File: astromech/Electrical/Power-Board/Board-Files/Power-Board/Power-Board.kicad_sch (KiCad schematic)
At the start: 74 parts, among them J1 BAT_IN_SCREW, J10 HEAD_MOT, J2 BAT_IN_HOLE, J5 E_STOP, J6 CTRL_BRD, J7 JETSON, J8 L_DRIVE, J9 R_DRIVE, Q1 Q_NMOS_DSG, Q2 Q_NMOS_DSG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

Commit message: assigned some footprints
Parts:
- 12V1, 12V2, 12V3, 12V4, 3.3V1, 3.3V2, 3.3V3, 3.3V4, 5V1, 5V2, 5V3, 5V4: footprint (none) -> astromech-footprints:Phoenix-1935161
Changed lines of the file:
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@@
       (effects (font (size 1.27 1.27)) (justify left))
     )
-    (property "Footprint" "" (id 2) (at 262.89 138.43 0)
+    (property "Footprint" "astromech-footprints:Phoenix-1935161" (id 2) (at 262.89 138.43 0)
       (effects (font (size 1.27 1.27)) hide)
     )
@@
       (effects (font (size 1.27 1.27)) (justify left))
     )
-    (property "Footprint" "" (id 2) (at 262.89 151.13 0)
+    (property "Footprint" "astromech-footprints:Phoenix-1935161" (id 2) (at 262.89 151.13 0)
       (effects (font (size 1.27 1.27)) hide)
     )
@@
       (effects (font (size 1.27 1.27)) (justify left))
     )
-    (property "Footprint" "" (id 2) (at 262.89 157.48 0)
+    (property "Footprint" "astromech-footprints:Phoenix-1935161" (id 2) (at 262.89 157.48 0)
       (effects (font (size 1.27 1.27)) hide)
     )
@@
       (effects (font (size 1.27 1.27)) (justify left))
     )
-    (property "Footprint" "" (id 2) (at 262.89 118.11 0)
+    (property "Footprint" "astromech-footprints:Phoenix-1935161" (id 2) (at 262.89 118.11 0)
       (effects (font (size 1.27 1.27)) hide)
     )
@@
       (effects (font (size 1.27 1.27)) (justify left))
     )
-    (property "Footprint" "" (id 2) (at 262.89 104.14 0)
+    (property "Footprint" "astromech-footprints:Phoenix-1935161" (id 2) (at 262.89 104.14 0)
       (effects (font (size 1.27 1.27)) hide)
     )
@@
       (effects (font (size 1.27 1.27)) (justify left))
     )
-    (property "Footprint" "" (id 2) (at 262.89 91.44 0)
+    (property "Footprint" "astromech-footprints:Phoenix-1935161" (id 2) (at 262.89 91.44 0)
       (effects (font (size 1.27 1.27)) hide)
     )
@@
       (effects (font (size 1.27 1.27)) (justify left))
     )
-    (property "Footprint" "" (id 2) (at 262.89 85.09 0)
+    (property "Footprint" "astromech-footprints:Phoenix-1935161" (id 2) (at 262.89 85.09 0)
       (effects (font (size 1.27 1.27)) hide)
     )
@@
       (effects (font (size 1.27 1.27)) (justify left))
     )
-    (property "Footprint" "" (id 2) (at 262.89 97.79 0)
+    (property "Footprint" "astromech-footprints:Phoenix-1935161" (id 2) (at 262.89 97.79 0)
       (effects (font (size 1.27 1.27)) hide)
     )
@@
       (effects (font (size 1.27 1.27)) (justify left))
     )
-    (property "Footprint" "" (id 2) (at 262.89 130.81 0)
+    (property "Footprint" "astromech-footprints:Phoenix-1935161" (id 2) (at 262.89 130.81 0)
       (effects (font (size 1.27 1.27)) hide)
     )
@@
       (effects (font (size 1.27 1.27)) (justify left))
     )
-    (property "Footprint" "" (id 2) (at 262.89 144.78 0)
+    (property "Footprint" "astromech-footprints:Phoenix-1935161" (id 2) (at 262.89 144.78 0)
       (effects (font (size 1.27 1.27)) hide)
     )
@@
       (effects (font (size 1.27 1.27)) (justify left))
     )
-    (property "Footprint" "" (id 2) (at 262.89 111.76 0)
+    (property "Footprint" "astromech-footprints:Phoenix-1935161" (id 2) (at 262.89 111.76 0)
       (effects (font (size 1.27 1.27)) hide)
     )
@@
       (effects (font (size 1.27 1.27)) (justify left))
     )
-    (property "Footprint" "" (id 2) (at 262.89 124.46 0)
+    (property "Footprint" "astromech-footprints:Phoenix-1935161" (id 2) (at 262.89 124.46 0)
       (effects (font (size 1.27 1.27)) hide)
     )
@@
     )
     (path "/9bcc4443-db93-4d21-84f6-322e2ec99325"
-      (reference "3.3V1") (unit 1) (value "Generic_Power_Out") (footprint "")
+      (reference "3.3V1") (unit 1) (value "Generic_Power_Out") (footprint "astromech-footprints:Phoenix-1935161")
     )
     (path "/9111e1c3-f841-4de6-a6b5-6bce4d1742f3"
-      (reference "3.3V2") (unit 1) (value "Generic_Power_Out") (footprint "")
+      (reference "3.3V2") (unit 1) (value "Generic_Power_Out") (footprint "astromech-footprints:Phoenix-1935161")
     )
     (path "/a10238b9-63a1-4997-a6e0-4b9a5f566bbf"
-      (reference "3.3V3") (unit 1) (value "Generic_Power_Out") (footprint "")
+      (reference "3.3V3") (unit 1) (value "Generic_Power_Out") (footprint "astromech-footprints:Phoenix-1935161")
     )
     (path "/89994059-2a1c-4ddc-8b41-cd0e03d88624"
-      (reference "3.3V4") (unit 1) (value "Generic_Power_Out") (footprint "")
+      (reference "3.3V4") (unit 1) (value "Generic_Power_Out") (footprint "astromech-footprints:Phoenix-1935161")
     )
     (path "/e3a5cde4-3039-4bc5-b9fc-befd33ed4d63"
-      (reference "5V1") (unit 1) (value "Generic_Power_Out") (footprint "")
+      (reference "5V1") (unit 1) (value "Generic_Power_Out") (footprint "astromech-footprints:Phoenix-1935161")
     )
     (path "/5a7955ad-2e24-4e7d-b479-f7b876c90d98"
-      (reference "5V2") (unit 1) (value "Generic_Power_Out") (footprint "")
+      (reference "5V2") (unit 1) (value "Generic_Power_Out") (footprint "astromech-footprints:Phoenix-1935161")
     )
     (path "/e6fb4523-8c9f-407d-8adf-aa8f2608bfd2"
-      (reference "5V3") (unit 1) (value "Generic_Power_Out") (footprint "")
+      (reference "5V3") (unit 1) (value "Generic_Power_Out") (footprint "astromech-footprints:Phoenix-1935161")
     )
     (path "/bc88c6f4-5ee7-4bec-ac65-06448f62b249"
-      (reference "5V4") (unit 1) (value "Generic_Power_Out") (footprint "")
+      (reference "5V4") (unit 1) (value "Generic_Power_Out") (footprint "astromech-footprints:Phoenix-1935161")
     )
     (path "/0d15a5b2-3e70-412b-9f36-a4c63baa566d"
-      (reference "12V1") (unit 1) (value "Generic_Power_Out") (footprint "")
+      (reference "12V1") (unit 1) (value "Generic_Power_Out") (footprint "astromech-footprints:Phoenix-1935161")
     )
     (path "/e04bb5c1-b97d-44fa-8824-8227d80fb6e7"
-      (reference "12V2") (unit 1) (value "Generic_Power_Out") (footprint "")
+      (reference "12V2") (unit 1) (value "Generic_Power_Out") (footprint "astromech-footprints:Phoenix-1935161")
     )
     (path "/1c649b9b-cecf-405e-925d-0c055c588218"
-      (reference "12V3") (unit 1) (value "Generic_Power_Out") (footprint "")
+      (reference "12V3") (unit 1) (value "Generic_Power_Out") (footprint "astromech-footprints:Phoenix-1935161")
     )
     (path "/5781368b-b530-47a7-9310-28a772b7c299"
-      (reference "12V4") (unit 1) (value "Generic_Power_Out") (footprint "")
+      (reference "12V4") (unit 1) (value "Generic_Power_Out") (footprint "astromech-footprints:Phoenix-1935161")
     )
     (path "/cad4d12f-4e2b-4c01-83f0-cba1304a8be3"

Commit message: Assigned more footprints
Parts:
- C1, C2, C3, C4, C5, C6, C7, C8: footprint (none) -> Capacitor_SMD:C_1206_3216Metric_Pad1.33x1.80mm_HandSolder
- F1: footprint (none) -> Fuse:Fuseholder_Blade_Mini_Keystone_3568
- HV_OUT1, HV_OUT2, HV_OUT3, HV_OUT4, J10, J5, J6, J7, J8, J9, LV_IN1, LV_IN2, LV_IN3, LV_IN4: footprint (none) -> astromech-footprints:Phoenix-1935161
- J1: footprint (none) -> astromech-footprints:Molex-393900102
- J2: footprint (none) -> astromech-footprints:10AWG-Power-In
- R1, R10, R11, R12, R2, R3, R4, R5, R6, R7, R8, R9: footprint (none) -> Resistor_SMD:R_1206_3216Metric_Pad1.30x1.75mm_HandSolder

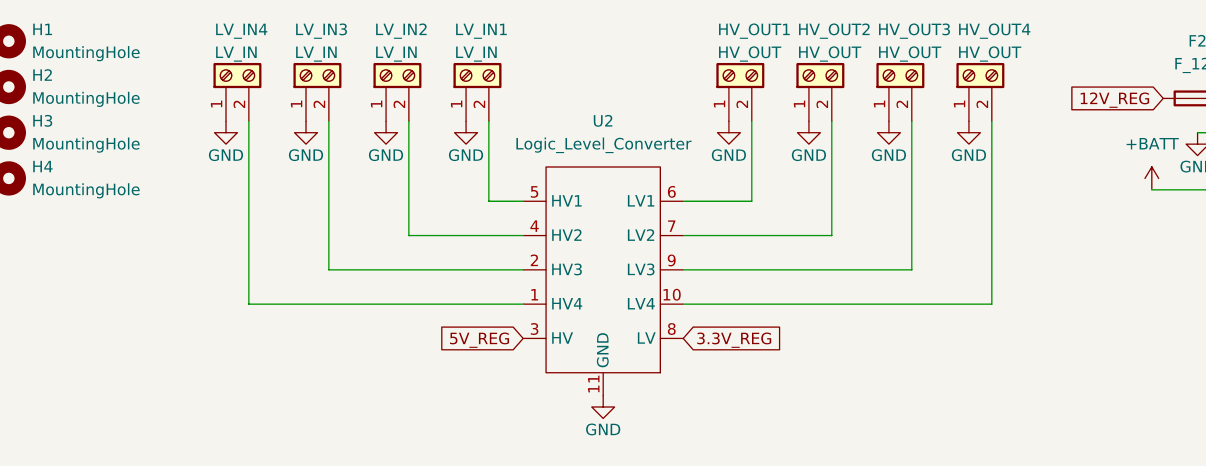
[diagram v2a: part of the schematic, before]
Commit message: Fixed level shifter mis-wiring
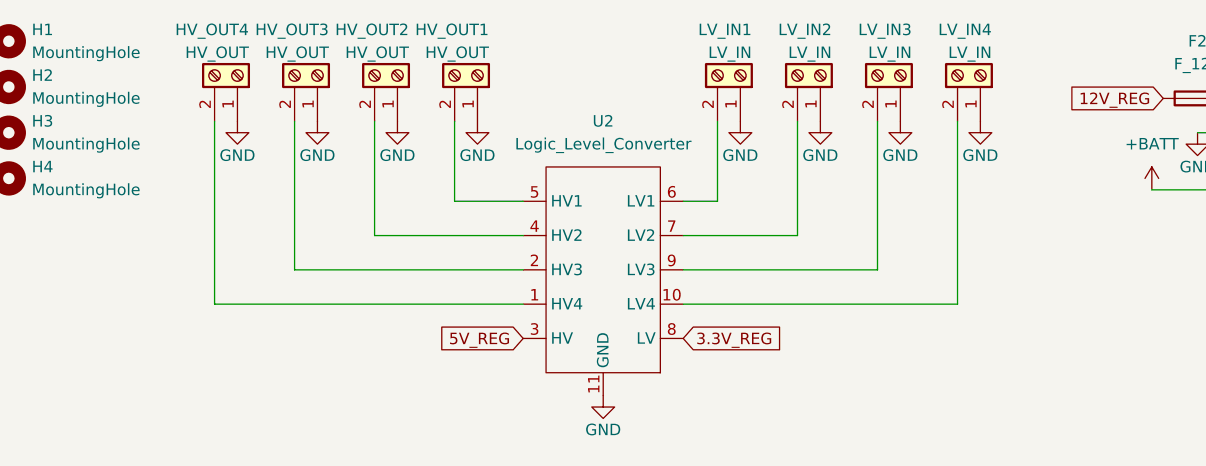
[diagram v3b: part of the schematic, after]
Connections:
- net at HV_OUT2.2 (Pin_2): now also U2.4 (HV2); no longer U2.7 (LV2)
- net at LV_IN1.2 (Pin_2): now also U2.6 (LV1); no longer U2.5 (HV1)
- net at HV_OUT4.2 (Pin_2): now also U2.1 (HV4); no longer U2.10 (LV4)
- net at LV_IN4.2 (Pin_2): now also U2.10 (LV4); no longer U2.1 (HV4)
- net at U2.2 (HV3): now also HV_OUT3.2 (Pin_2); no longer LV_IN3.2 (Pin_2)
- net at LV_IN2.2 (Pin_2): now also U2.7 (LV2); no longer U2.4 (HV2)
- net at HV_OUT1.2 (Pin_2): now also U2.5 (HV1); no longer U2.6 (LV1)
- net at U2.9 (LV3): now also LV_IN3.2 (Pin_2); no longer HV_OUT3.2 (Pin_2)
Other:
- moved on the sheet: HV_OUT1, HV_OUT2, HV_OUT3, HV_OUT4, LV_IN1, LV_IN2, LV_IN3, LV_IN4

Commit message: loaded components into board
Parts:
- TP1, TP2: footprint (none) -> TestPoint:TestPoint_Pad_D2.0mm
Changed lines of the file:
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@@
       (effects (font (size 1.27 1.27)) (justify right))
     )
-    (property "Footprint" "" (id 2) (at 78.74 173.99 0)
+    (property "Footprint" "TestPoint:TestPoint_Pad_D2.0mm" (id 2) (at 78.74 173.99 0)
       (effects (font (size 1.27 1.27)) hide)
     )
@@
       (effects (font (size 1.27 1.27)) (justify right))
     )
-    (property "Footprint" "" (id 2) (at 190.5 153.67 0)
+    (property "Footprint" "TestPoint:TestPoint_Pad_D2.0mm" (id 2) (at 190.5 153.67 0)
       (effects (font (size 1.27 1.27)) hide)
     )
@@
     )
     (path "/50661fd7-fa27-4270-9a92-8cc6e80783d5"
-      (reference "TP1") (unit 1) (value "TestPoint") (footprint "")
+      (reference "TP1") (unit 1) (value "TestPoint") (footprint "TestPoint:TestPoint_Pad_D2.0mm")
     )
     (path "/9e399eee-ad6f-4fbe-bdf3-b9dd3880e86f"
-      (reference "TP2") (unit 1) (value "TestPoint") (footprint "")
+      (reference "TP2") (unit 1) (value "TestPoint") (footprint "TestPoint:TestPoint_Pad_D2.0mm")
     )
     (path "/a8721d09-e6f1-43a5-9f1e-a0052ba03c26"

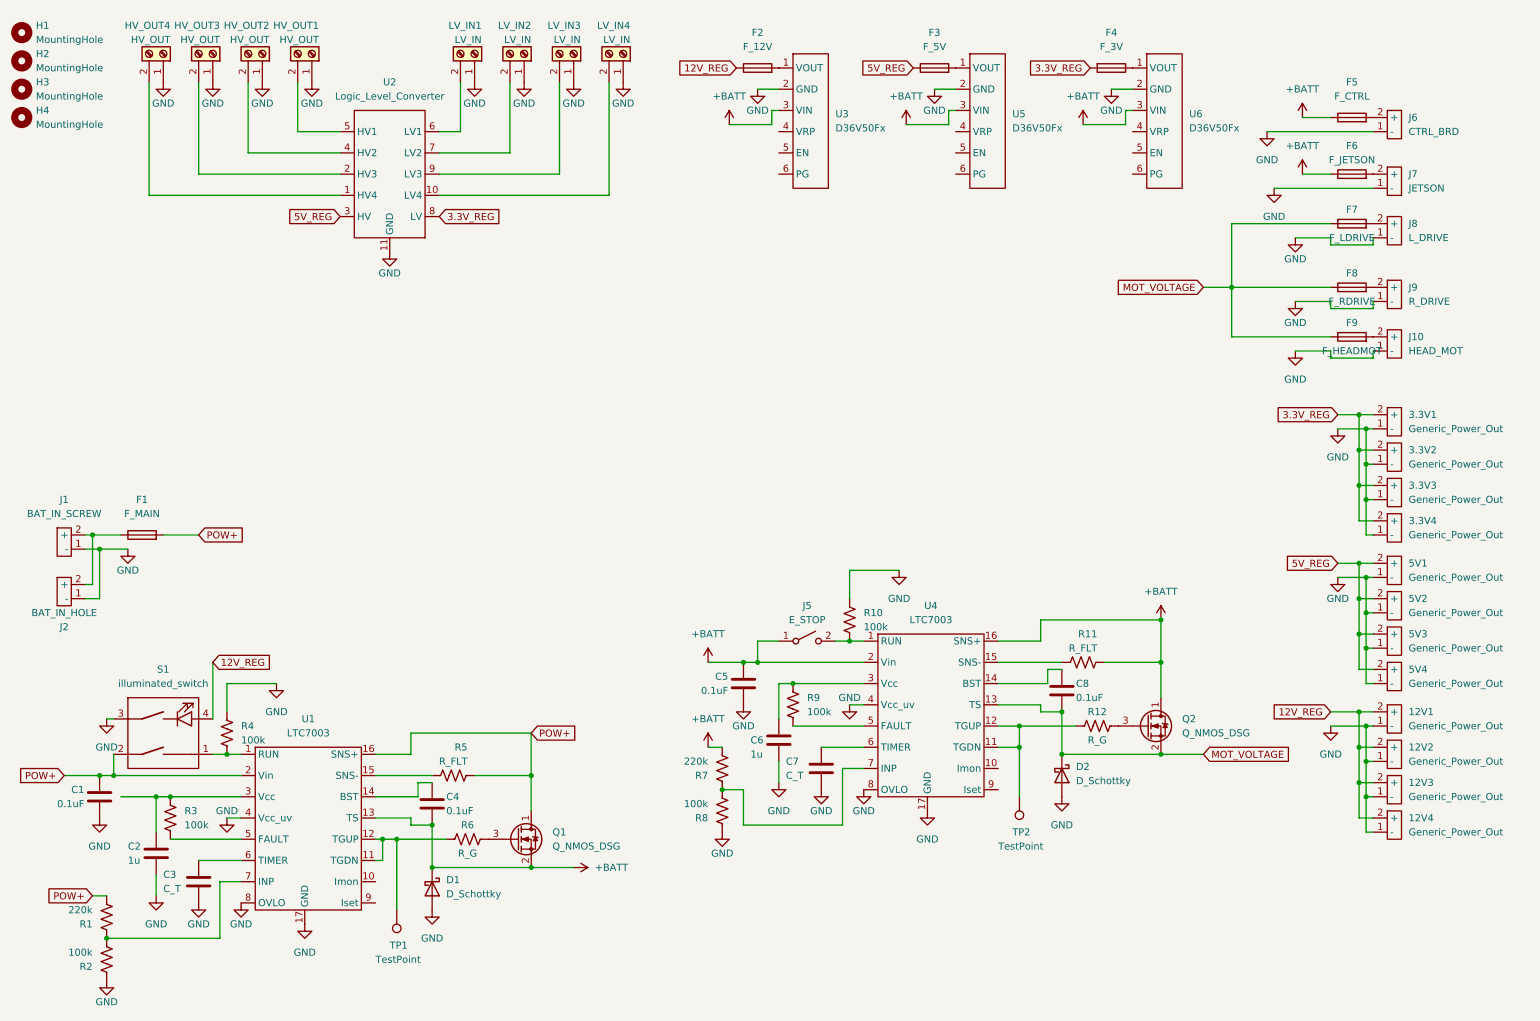
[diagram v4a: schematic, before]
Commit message: grouped related components and did minor layout
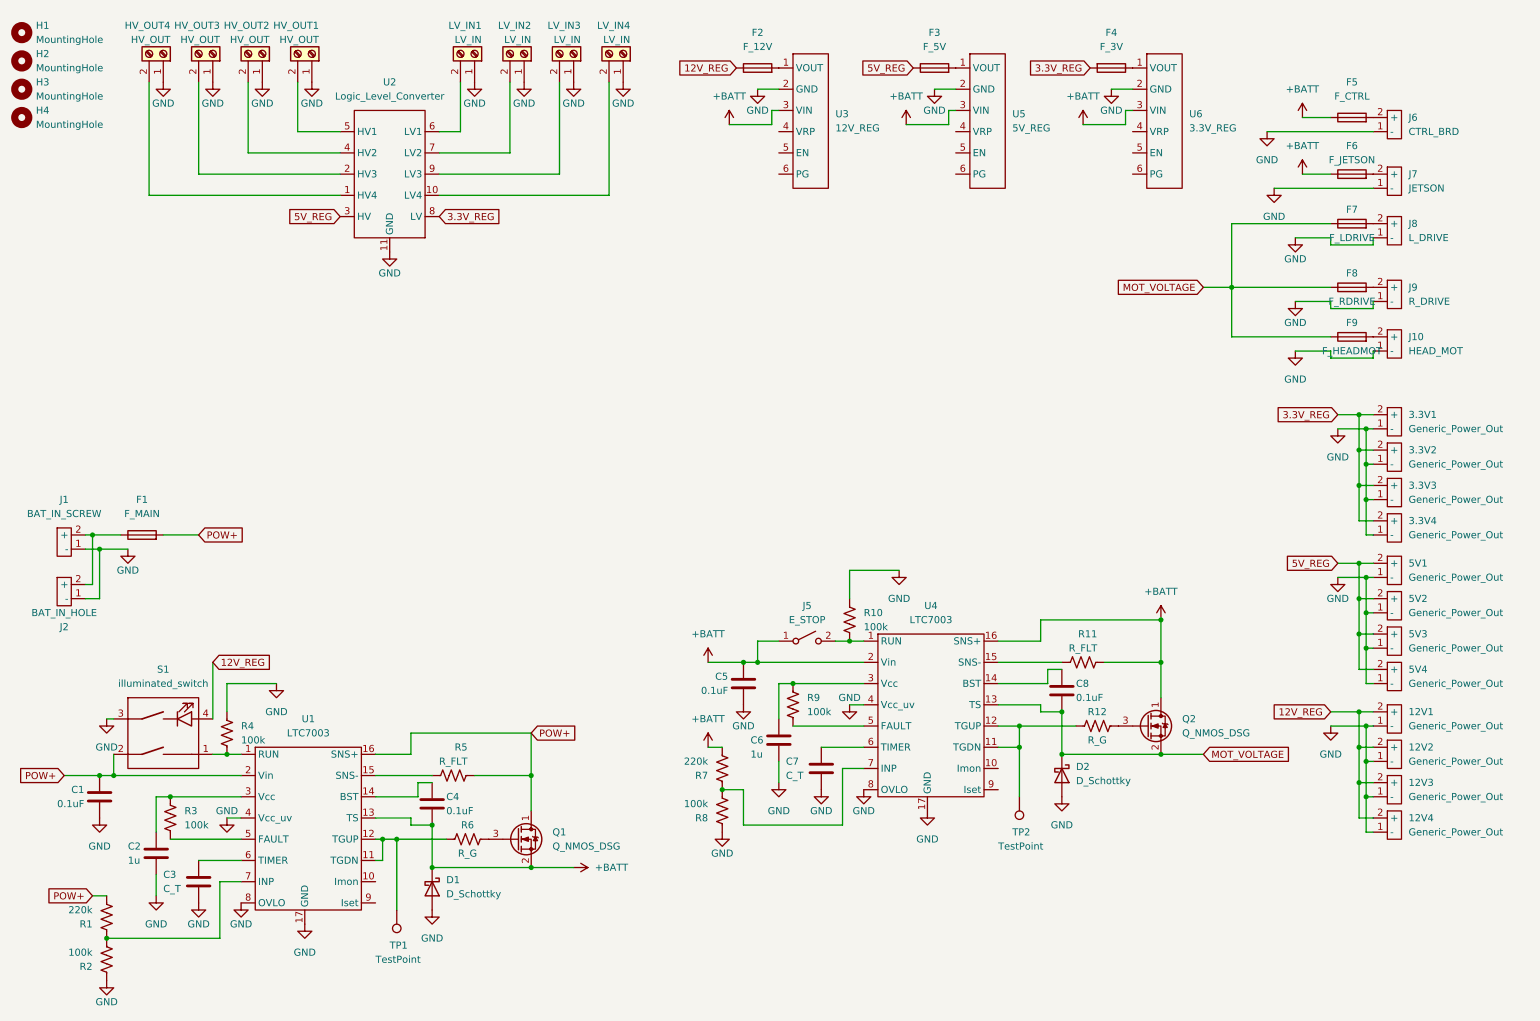
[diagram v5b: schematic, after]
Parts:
- U3: value D36V50Fx -> 12V_REG
- U5: value D36V50Fx -> 5V_REG
- U6: value D36V50Fx -> 3.3V_REG
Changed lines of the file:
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@@
   (junction (at 256.54 91.44) (diameter 0) (color 0 0 0 0)
   )
-  (junction (at 40.64 153.67) (diameter 0) (color 0 0 0 0)
-  )
   (junction (at 31.75 179.07) (diameter 0) (color 0 0 0 0)
   )
@@
     (stroke (width 0) (type default) (color 0 0 0 0))
   )
-  (wire (pts (xy 34.29 153.67) (xy 40.64 153.67))
-    (stroke (width 0) (type default) (color 0 0 0 0))
-  )
   (wire (pts (xy 259.08 53.34) (xy 259.08 54.61))
     (stroke (width 0) (type default) (color 0 0 0 0))
@@
       (effects (font (size 1.27 1.27)) (justify left))
     )
-    (property "Value" "D36V50Fx" (id 1) (at 194.31 33.6549 0)
+    (property "Value" "5V_REG" (id 1) (at 194.31 33.6549 0)
       (effects (font (size 1.27 1.27)) (justify left))
     )
@@
       (effects (font (size 1.27 1.27)) (justify left))
     )
-    (property "Value" "D36V50Fx" (id 1) (at 226.06 33.6549 0)
+    (property "Value" "3.3V_REG" (id 1) (at 226.06 33.6549 0)
       (effects (font (size 1.27 1.27)) (justify left))
     )
@@
       (effects (font (size 1.27 1.27)) (justify left))
     )
-    (property "Value" "D36V50Fx" (id 1) (at 162.56 33.6549 0)
+    (property "Value" "12V_REG" (id 1) (at 162.56 33.6549 0)
       (effects (font (size 1.27 1.27)) (justify left))
     )
@@
     )
     (path "/efbdab35-fea1-49fc-a788-137897379b0d"
-      (reference "U3") (unit 1) (value "D36V50Fx") (footprint "astromech-footprints:D36V50Fx")
+      (reference "U3") (unit 1) (value "12V_REG") (footprint "astromech-footprints:D36V50Fx")
     )
     (path "/0b5c0b2b-fb81-40d7-ba95-17c4d4c6112c"
@@
     )
     (path "/239f3797-1bc5-4e51-b93a-8ccf9de596cf"
-      (reference "U5") (unit 1) (value "D36V50Fx") (footprint "astromech-footprints:D36V50Fx")
+      (reference "U5") (unit 1) (value "5V_REG") (footprint "astromech-footprints:D36V50Fx")
     )
     (path "/b90d7ced-c107-4650-987d-af45d91d2eed"
-      (reference "U6") (unit 1) (value "D36V50Fx") (footprint "astromech-footprints:D36V50Fx")
+      (reference "U6") (unit 1) (value "3.3V_REG") (footprint "astromech-footprints:D36V50Fx")
     )
   )
